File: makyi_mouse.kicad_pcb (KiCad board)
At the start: 2 copper layers, 60 x 78.5 mm, 114 parts, among them J1 Conn_01x02_Pin, J10 Conn_01x06_Pin, J11 Conn_01x06_Pin, J12 Conn_01x06_Pin, J13 Conn_01x06_Pin, J14 20021221-00006C4LF, J2 Conn_01x04_Pin, J3 Conn_01x04_Pin, J4 Conn_01x04_Pin, J5 Conn_01x04_Pin, J6 Conn_01x04_Pin, J7 Conn_01x04_Pin, J8 Conn_01x04_Pin, J9 Conn_01x04_Pin, M1 Motor_DC, M2 Motor_DC, Q1 DMN63D8L-7, Q2 GSFC02A05, Q3 LTR-4206, Q4 LTR-4206, Q5 LTR-4206, Q6 LTR-4206, SW1 AYZ0102AGRLC, SW2 C5143614, SW3 C5143614, U1 NCP177AMX330TCG, U10 MB85RC64TAPN-G-AMEWE1, U11 STM32H573RIVx, U12 INA210, U14 INA210, U2 ICM-42688-P, U3 DRV8836DSSR, U4 BCR421UW6-7, U5 BCR421UW6-7, U6 BCR421UW6-7, U7 BCR421UW6-7, U8 MA730, U9 MA730

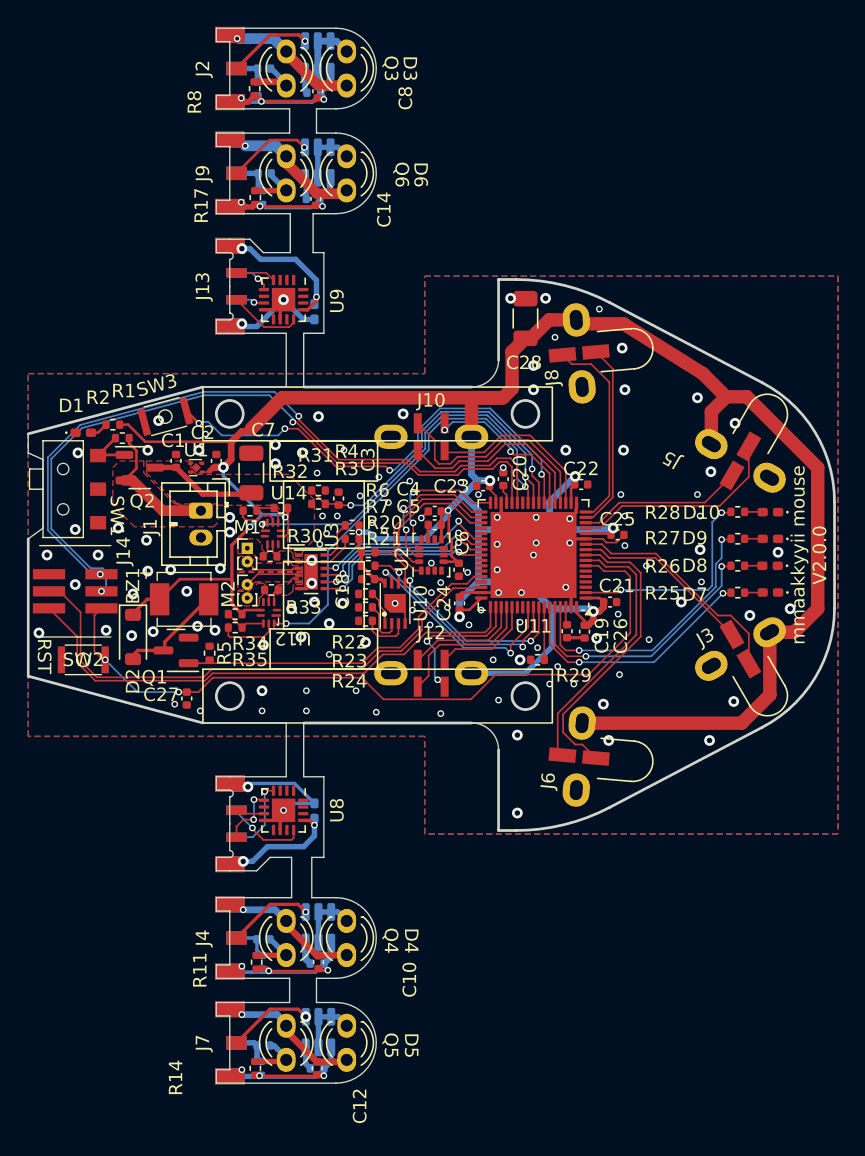
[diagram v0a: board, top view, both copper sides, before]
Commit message: 壁センサ修正
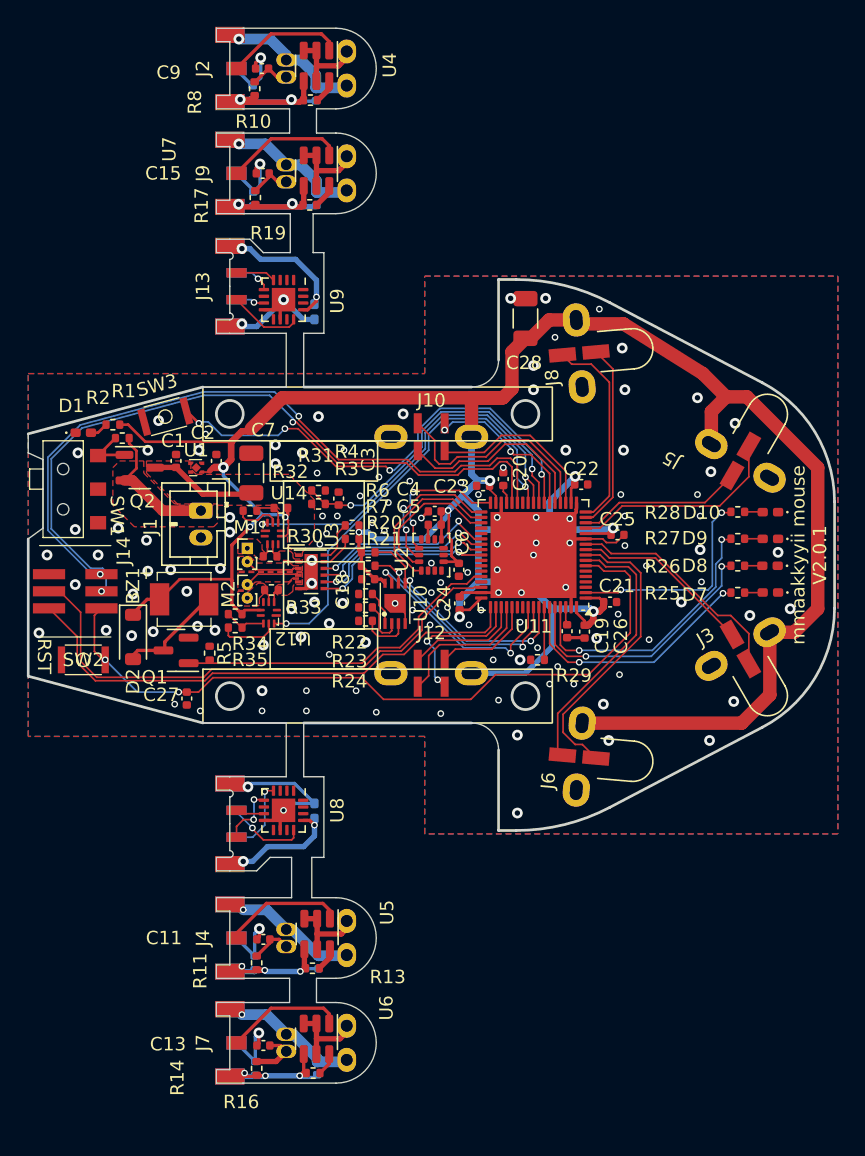
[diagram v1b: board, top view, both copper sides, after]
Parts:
- C10, C12, C14, C8, D3, D4, D5, D6: moved to B.Cu
- C11, C13, C15, C9: value 1u -> 0.1u; moved to F.Cu
- C16, C17: value C -> 0.1u
- Q3, Q4, Q5, Q6: value LTR-4206 -> OP505A; footprint makyi_mouse:LED -> makyi_mouse:LED_photo_tr; moved to B.Cu
- R10, R13, R16, R19, U4, U5, U6, U7: moved to F.Cu
- R11, R14, R17, R8: value 4.3k -> 1.5k
- R12, R15, R18, R9: value 4.3k -> 10k
- R30, R31, R32, R33, R34, R35: value R -> 10k
- U10: value MB85RC64TAPN-G-AMEWE1 -> v
- moved U4 0.71 mm to (141.4, 43.6)
- moved R18 0.66 mm to (136.8, 53.5)
- moved U7 0.61 mm to (141.4, 51.4)
- moved R10 0.60 mm to (141.0, 46.1), turned to 0 degrees
- moved R12 0.55 mm to (136.8, 110.3)
- moved U6 0.52 mm to (141.4, 116.0)
- moved R19 0.51 mm to (140.9, 54.0), turned to 0 degrees
- moved U5 0.51 mm to (141.5, 108.2)
- moved R13 0.49 mm to (141.2, 110.8), turned to 0 degrees
- moved R9 0.46 mm to (136.7, 45.6)
- moved R16 0.46 mm to (141.2, 118.5), turned to 0 degrees
- moved R15 0.40 mm to (136.9, 118.2)
- moved C8 0.27 mm to (141.4, 45.7)
- moved C15 0.15 mm to (137.4, 51.6)
- moved C9 0.15 mm to (137.4, 43.8)
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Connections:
- net Net-(D3-A) renamed /wall_sensor/ENC_3.3V
- net Net-(D4-A) renamed /wall_sensor1/ENC_3.3V
- net Net-(D5-A) renamed /wall_sensor2/ENC_3.3V
- net Net-(D6-A) renamed /wall_sensor3/ENC_3.3V
- net Net-(J2-Pin_1) renamed /wall_sensor/ENC_LED
- net Net-(J2-Pin_2) renamed /wall_sensor/ENC_OUT
- net Net-(J2-Pin_3) renamed /wall_sensor/ENC_GND
- net Net-(J4-Pin_1) renamed /wall_sensor1/ENC_LED
- net Net-(J4-Pin_2) renamed /wall_sensor1/ENC_OUT
- net Net-(J4-Pin_3) renamed /wall_sensor1/ENC_GND
- net Net-(J7-Pin_1) renamed /wall_sensor2/ENC_LED
- net Net-(J7-Pin_2) renamed /wall_sensor2/ENC_OUT
- net Net-(J7-Pin_3) renamed /wall_sensor2/ENC_GND
- net Net-(J9-Pin_1) renamed /wall_sensor3/ENC_LED
- net Net-(J9-Pin_2) renamed /wall_sensor3/ENC_OUT
- net Net-(J9-Pin_3) renamed /wall_sensor3/ENC_GND
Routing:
- net /wall_sensor1/ENC_GND: track 15.8 -> 11.0 mm
- net /wall_sensor2/ENC_GND: track 15.0 -> 12.0 mm
- net /wall_sensor1/ENC_LED: track 6.42 -> 9.05 mm, vias 1 -> 0
- net /wall_sensor3/ENC_LED: track 6.30 -> 8.90 mm, vias 1 -> 0
- net /wall_sensor/ENC_LED: track 6.33 -> 8.87 mm, vias 1 -> 0
- net /wall_sensor/ENC_OUT: track 2.57 -> 5.08 mm, vias 0 -> 1
- net /wall_sensor2/ENC_LED: track 6.42 -> 8.86 mm, vias 1 -> 0
- net /wall_sensor/ENC_3.3V: track 9.54 -> 12.0 mm
- net /wall_sensor2/ENC_OUT: track 2.91 -> 5.31 mm, vias 0 -> 1
- net /wall_sensor1/ENC_OUT: track 2.91 -> 4.96 mm, vias 0 -> 1
- net /wall_sensor3/ENC_OUT: track 3.03 -> 5.02 mm, vias 0 -> 1
- net /wall_sensor3/ENC_GND: track 14.8 -> 13.0 mm, vias 3 -> 2
- net Net-(D4-K): track 4.65 -> 6.16 mm
- net Net-(D6-K): track 4.70 -> 6.19 mm
- net Net-(D5-K): track 4.70 -> 6.15 mm
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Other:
- board text added: "mmaakkyyii mouse V2.0.1"
- board text removed: "mmaakkyyii mouse V2.0.0"
